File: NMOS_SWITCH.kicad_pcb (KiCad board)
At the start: 2 copper layers, 35 x 25 mm, 22 parts, among them J1 Conn_01x02, J2 Conn_01x02, J3 Conn_01x02, Q1 Q_NPN_BCE, Q2 CSD18540Q5B, U1 BTS443P, U2 LM5050-1

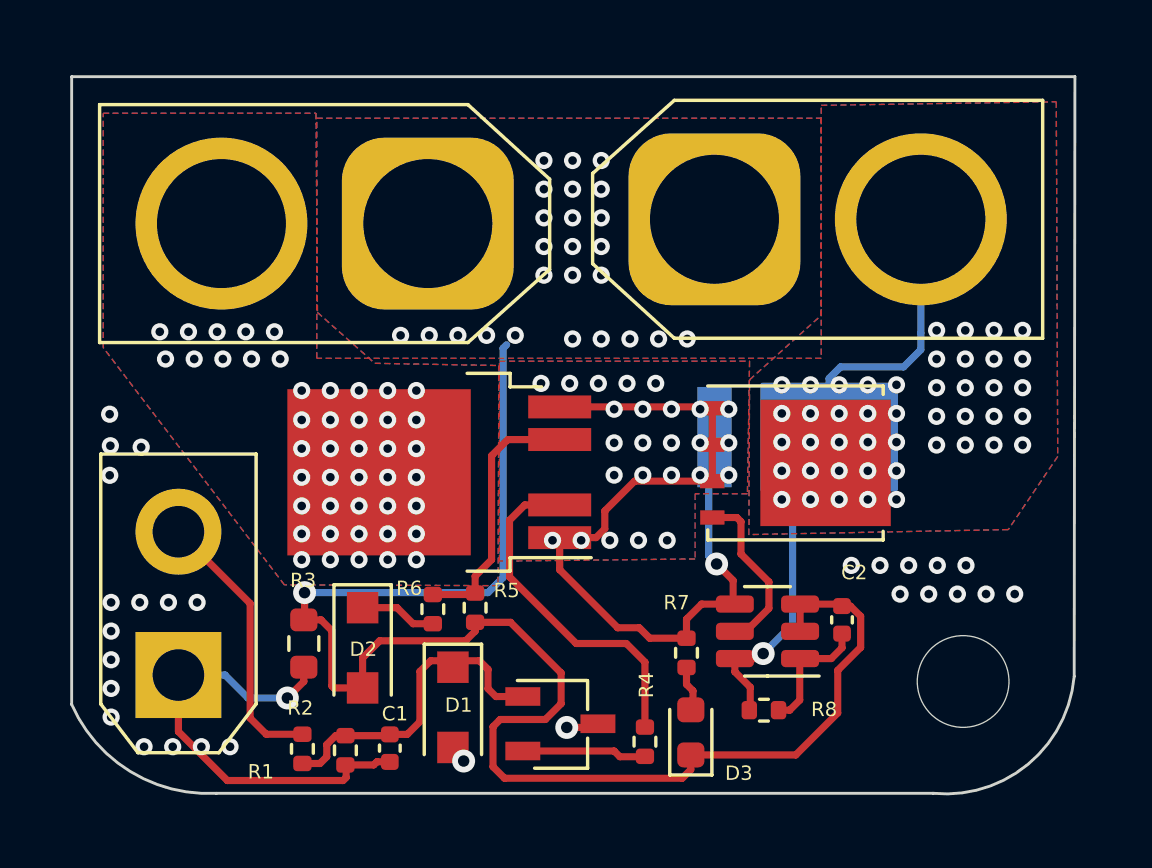
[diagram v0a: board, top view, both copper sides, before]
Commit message: Add time delay
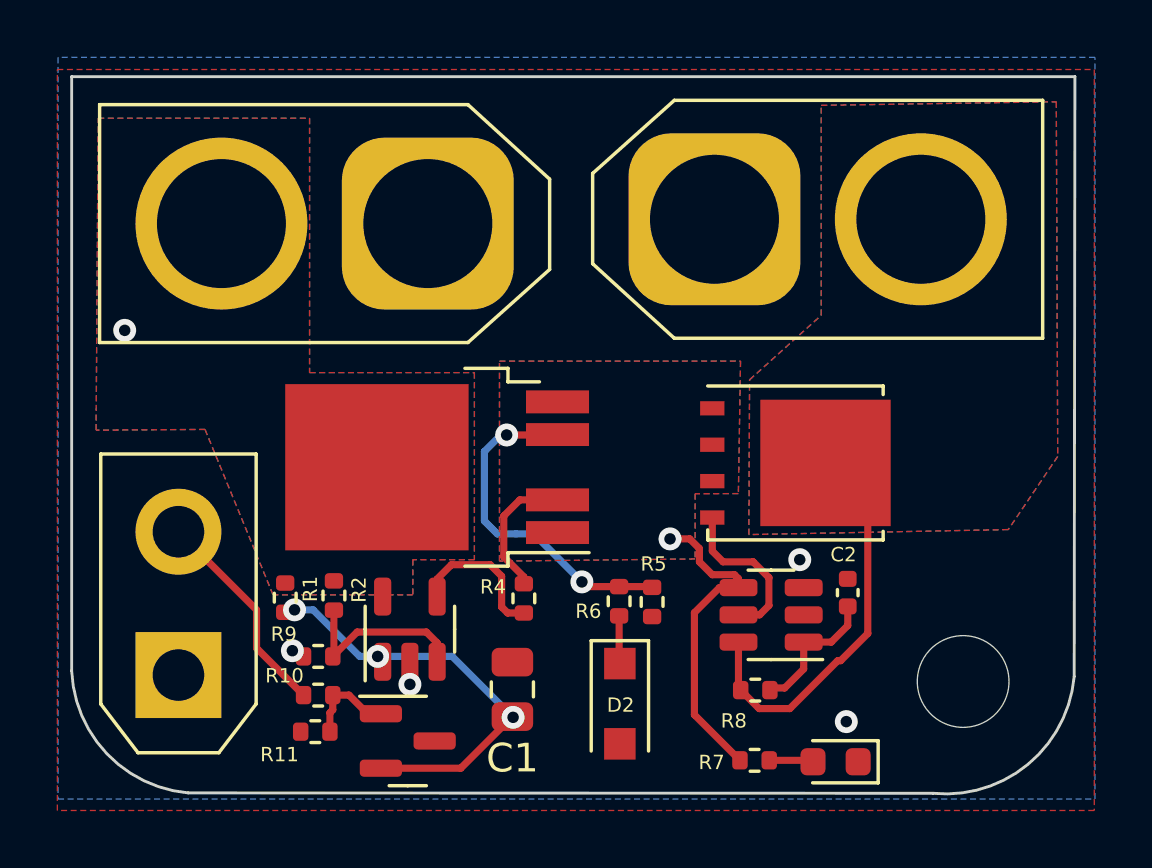
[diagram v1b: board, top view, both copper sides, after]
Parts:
- removed D1: BZT52Bxx, Diode_SMD:D_SOD-123F
- removed D4: SVM1550UB, POWER_DIODE_SMD:TO-277A
- removed R3: 0, Resistor_SMD:R_0603_1608Metric
- added R10: 10k, Resistor_SMD:R_0402_1005Metric, F.Cu at (147.2, 104.0)
- added R11: 100k, Resistor_SMD:R_0402_1005Metric, F.Cu at (147.1, 105.3)
- added R9: 47k, Resistor_SMD:R_0402_1005Metric, F.Cu at (147.2, 102.7)
- added U3: TL331, Package_TO_SOT_SMD:SOT-23-5, F.Cu at (150.4, 101.7)
- C1: value 104 -> 4.7u; footprint Capacitor_SMD:C_0402_1005Metric -> Capacitor_SMD:C_0805_2012Metric
- C2: value 104 -> 100n
- Q1: value Q_NPN_BCE -> Q_PNP_BEC; footprint Package_TO_SOT_SMD:TSOT-23 -> Package_TO_SOT_SMD:SOT-23
- R1: value 10k -> 210k
- R2: value 10k -> 6.8k
- R8: value 100R -> 100
- moved D2 9.18 mm to (157.7, 104.3)
- moved R4 6.55 mm to (154.4, 100.6)
- moved R6 6.51 mm to (157.7, 100.7)
- moved R5 6.18 mm to (158.8, 100.8)
- moved R2 5.41 mm to (147.8, 100.5)
- moved Q1 5.36 mm to (150.3, 105.6)
- moved R1 5.31 mm to (146.1, 100.6), turned to 90 degrees
- moved D3 5.15 mm to (165.2, 106.3), turned to 180 degrees
- moved C1 4.74 mm to (154.0, 103.8), turned to 90 degrees
- moved R7 4.44 mm to (162.4, 106.3), turned to 0 degrees
- moved C2 0.97 mm to (165.7, 100.4)
- moved R8 0.76 mm to (162.4, 103.8), turned to 180 degrees
- moved U2 0.59 mm to (163.0, 101.2)
- moved U1 0.19 mm to (151.3, 96.0)
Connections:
- C1 pad 1: Net-(C1-Pad1) -> Net-(U3-Pad1)
- C2 pad 1: Net-(C2-Pad1) -> Net-(U2-Pad1)
- C2 pad 2: GNDPWR -> GND
- D2 pad 2: GNDPWR -> GND
- D3 pad 1: GNDPWR -> GND
- J2 pad 1: GNDPWR -> GND
- J3 pad 1: GNDPWR -> GND
- Q1 pad 1: Net-(C1-Pad1) -> Net-(R10-Pad2)
- Q1 pad 2: Net-(Q1-Pad2) -> Net-(U3-Pad1)
- R1 pad 1: /EN -> Net-(U3-Pad1)
- R1 pad 2: Net-(C1-Pad1) -> /NMOS_IN
- R2 pad 1: Net-(C1-Pad1) -> /NMOS_IN
- R2 pad 2: GND -> Net-(U3-Pad3)
- R4 pad 1: Net-(Q1-Pad2) -> Net-(R4-Pad1)
- R5 pad 1: GNDPWR -> GND
- R8 pad 1: /NMOS_OUT -> Net-(U2-Pad1)
- R8 pad 2: Net-(C2-Pad1) -> /NMOS_OUT
- U2 pad 1: Net-(C2-Pad1) -> Net-(U2-Pad1)
- U2 pad 2: GNDPWR -> GND
- U2 pad 3: GNDPWR -> GND
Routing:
- net GNDPWR: track 55.5 -> 0.00 mm, vias 26 -> 0
- net GND: track 17.2 -> 0.00 mm, vias 29 -> 4
- net Net-(Q2-Pad1): track 28.0 -> 11.3 mm, vias 26 -> 1
- net Net-(U3-Pad1): track 0.00 -> 15.1 mm, vias 0 -> 3
- net Net-(C1-Pad1): track 11.4 -> 0.00 mm
- net /NMOS_OUT: track 22.7 -> 14.0 mm, vias 46 -> 0
- net Net-(R4-Pad2): track 12.2 -> 4.76 mm
- net Net-(U3-Pad3): track 0.00 -> 6.44 mm
- net Net-(R4-Pad1): track 0.00 -> 5.17 mm
- net Net-(U2-Pad1): track 0.00 -> 4.84 mm
- net Net-(C2-Pad1): track 4.45 -> 0.00 mm
- net Net-(Q1-Pad2): track 4.35 -> 0.00 mm
- net Net-(R10-Pad2): track 0.00 -> 3.46 mm
- net Net-(R5-Pad2): track 9.13 -> 12.0 mm, vias 0 -> 2
- net /EN: track 9.59 -> 7.51 mm
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- removed copper zone on B.Cu, net GNDPWR
- removed copper zone on F.Cu, net GNDPWR
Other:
- outline, holes or cut-outs redrawn
